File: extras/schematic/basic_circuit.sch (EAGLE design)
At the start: 2 parts, among them M1 ARDUINO-PRO-MINI-3.3V

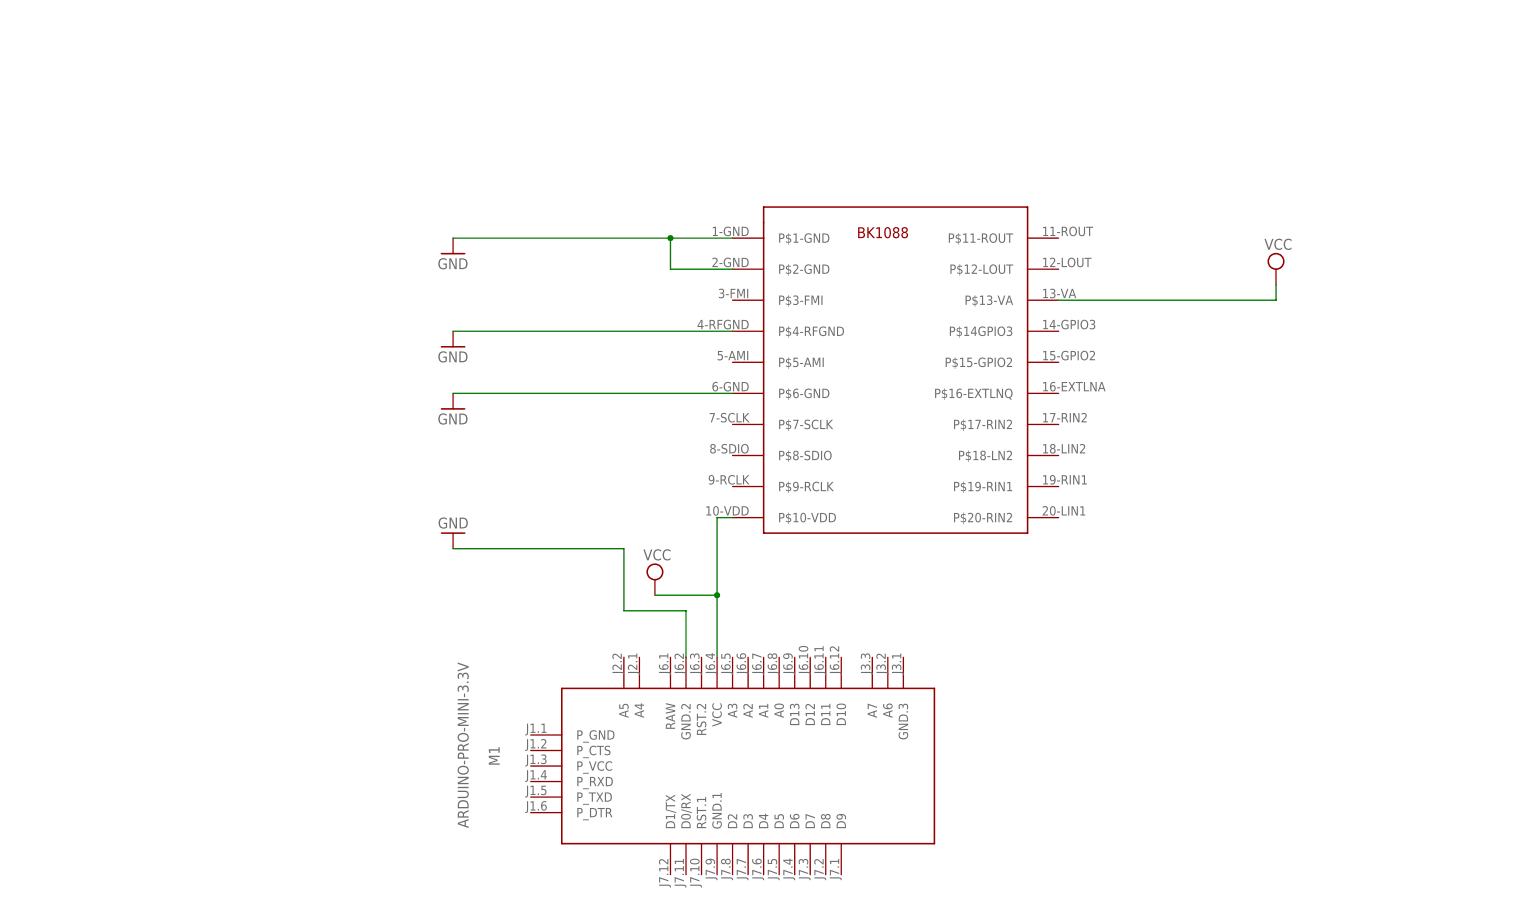
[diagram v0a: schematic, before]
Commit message: BK108X Arduino Library
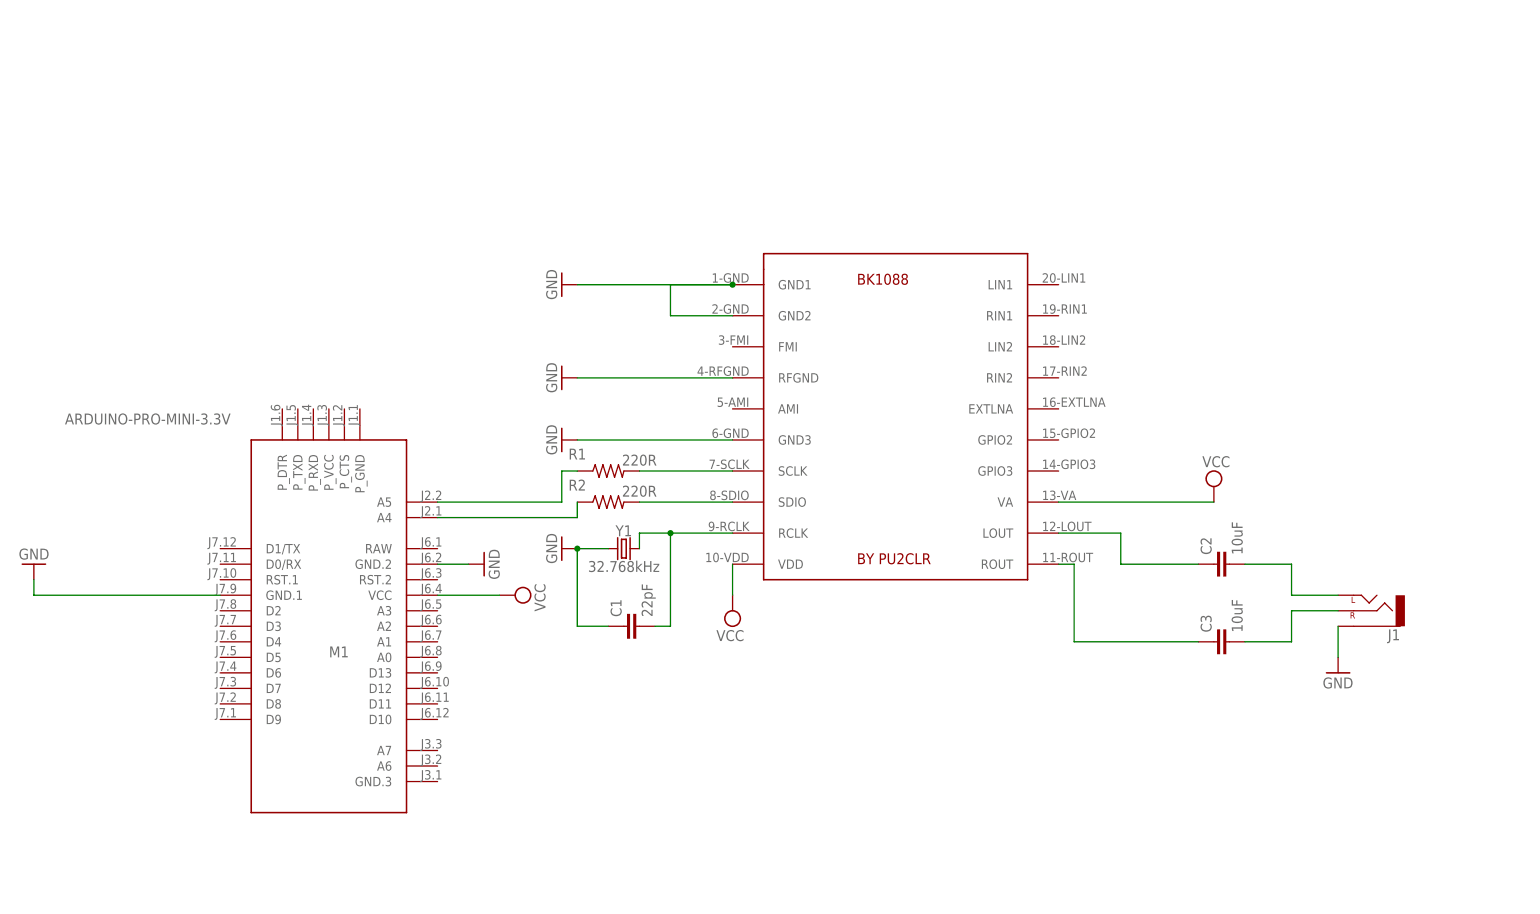
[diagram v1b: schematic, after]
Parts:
- added C1: 22pF, SparkFun-Capacitors:22PF-0603-50V-5%
- added C2, C3: 10uF, SparkFun-Capacitors:10UF-0603-6.3V-20%
- added J1: (no value), SparkFun-Connectors:AUDIO_JACK_2.5MMSPECIAL_POGO_PINS
- added R1, R2: 220R, Resistor:R-US_AXIAL-7.2MM-PITCH
- added Y1: 32.768kHz, SparkFun-Clocks:CRYSTAL-32.768KHZPTH-2X6
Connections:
- new net N$1: R1.2, U$1.SCLK
- new net N$2: R2.2, U$1.SDIO
- new net N$3: M1.A4, R2.1
- new net N$4: M1.A5, R1.1
- new net N$5: C1.2, U$1.RCLK, Y1.2
- new net N$6: C3.1, U$1.ROUT
- new net N$7: C2.1, U$1.LOUT
- new net N$8: C3.2, J1.RIGHT
- new net N$9: C2.2, J1.LEFT
- net GND: now also C1.1, J1.SLEEVE, M1.GND.1, U$1.GND1, U$1.GND2, U$1.GND3, U$1.RFGND, Y1.1; no longer U$1.P$1-GND, U$1.P$2-GND, U$1.P$4-RFGND, U$1.P$6-GND
- net VCC: now also U$1.VA, U$1.VDD; no longer U$1.P$10-VDD, U$1.P$13-VA
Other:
- moved on the sheet: M1

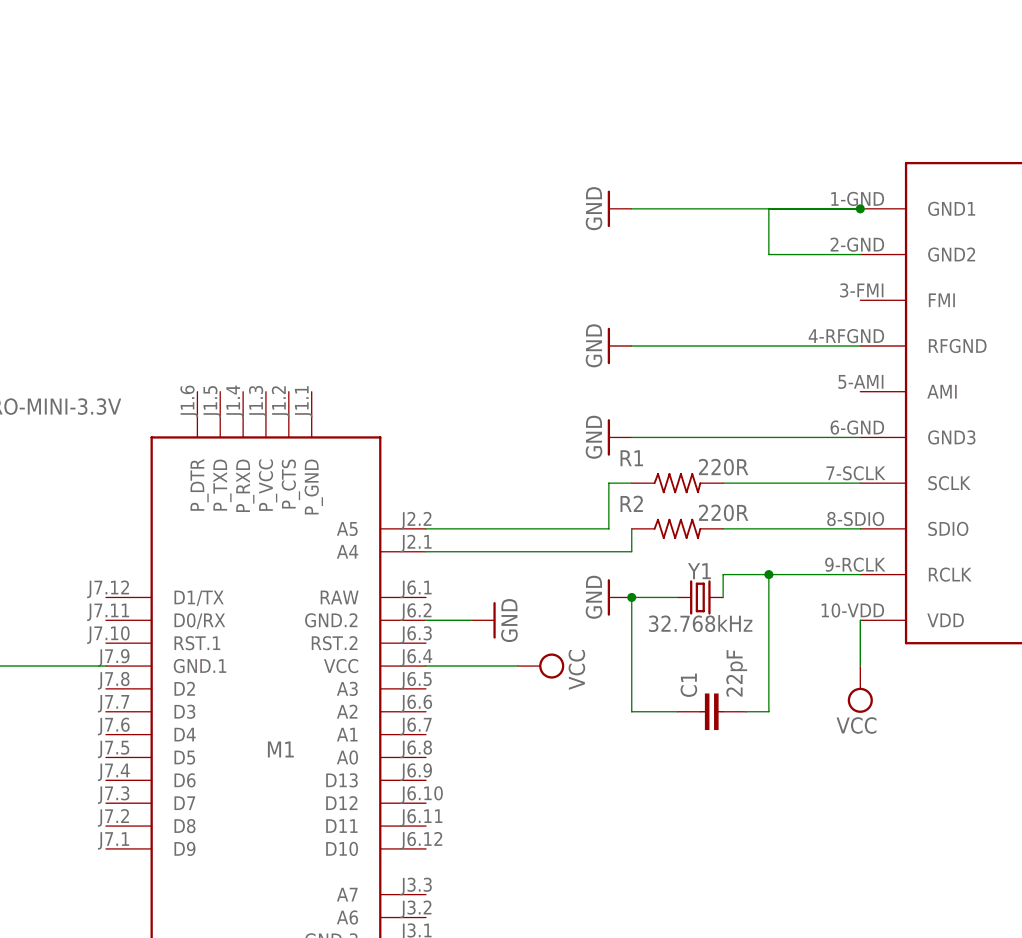
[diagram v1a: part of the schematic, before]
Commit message: BK1088 Arduino Library
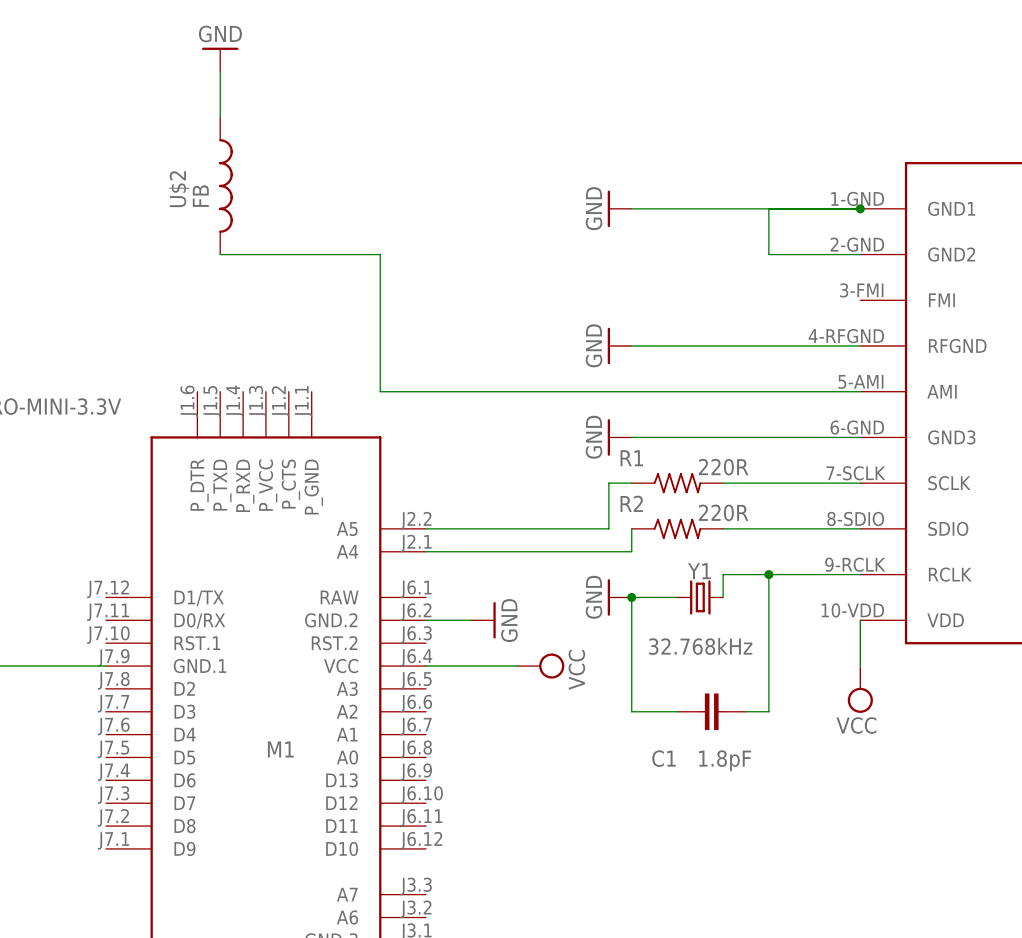
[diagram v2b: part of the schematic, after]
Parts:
- added U$2: FB, adafruit:FB
- C1: value 22pF -> 1.8pF; device SparkFun-Capacitors:22PF-0603-50V-5% -> capacitor-wima:C5/3
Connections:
- new net N$10: U$1.AMI, U$2.2
- net GND: now also U$2.1
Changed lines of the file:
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@@
 <part name="GND4" library="supply1" library_urn="urn:adsk.eagle:library:371" deviceset="GND" device=""/>
 <part name="Y1" library="SparkFun-Clocks" library_urn="urn:adsk.eagle:library:511" deviceset="CRYSTAL-32.768KHZ" device="PTH-2X6" package3d_urn="urn:adsk.eagle:package:37514/1" value="32.768kHz"/>
-<part name="C1" library="SparkFun-Capacitors" library_urn="urn:adsk.eagle:library:510" deviceset="22PF" device="-0603-50V-5%" package3d_urn="urn:adsk.eagle:package:37414/1" value="22pF"/>
 <part name="C2" library="SparkFun-Capacitors" library_urn="urn:adsk.eagle:library:510" deviceset="10UF" device="-0603-6.3V-20%" package3d_urn="urn:adsk.eagle:package:37414/1" value="10uF"/>
 <part name="C3" library="SparkFun-Capacitors" library_urn="urn:adsk.eagle:library:510" deviceset="10UF" device="-0603-6.3V-20%" package3d_urn="urn:adsk.eagle:package:37414/1" value="10uF"/>
@@
 <part name="SUPPLY1" library="supply2" library_urn="urn:adsk.eagle:library:372" deviceset="VCC" device=""/>
 <part name="GND7" library="supply1" library_urn="urn:adsk.eagle:library:371" deviceset="GND" device=""/>
+<part name="C1" library="capacitor-wima" library_urn="urn:adsk.eagle:library:116" deviceset="C" device="5/3" package3d_urn="urn:adsk.eagle:package:5433/1" value="1.8pF"/>
+<part name="U$2" library="adafruit" library_urn="urn:adsk.eagle:library:420" deviceset="FB" device="" package3d_urn="urn:adsk.eagle:package:6240653/1"/>
+<part name="GND8" library="supply1" library_urn="urn:adsk.eagle:library:371" deviceset="GND" device=""/>
 </parts>
 <sheets>
@@
 <instance part="Y1" gate="G$1" x="30.48" y="33.02" smashed="yes">
 <attribute name="NAME" x="30.48" y="35.052" size="1.778" layer="95" font="vector" align="bottom-center"/>
-<attribute name="VALUE" x="30.48" y="30.988" size="1.778" layer="96" font="vector" align="top-center"/>
-</instance>
-<instance part="C1" gate="G$1" x="33.02" y="20.32" smashed="yes" rot="R90">
-<attribute name="NAME" x="30.099" y="21.844" size="1.778" layer="95" font="vector" rot="R90"/>
-<attribute name="VALUE" x="35.179" y="21.844" size="1.778" layer="96" font="vector" rot="R90"/>
+<attribute name="VALUE" x="30.48" y="28.448" size="1.778" layer="96" font="vector" align="top-center"/>
 </instance>
 <instance part="C2" gate="G$1" x="129.54" y="30.48" smashed="yes" rot="R90">
@@
 <instance part="GND7" gate="1" x="7.62" y="30.48" smashed="yes" rot="R90">
 <attribute name="VALUE" x="10.16" y="27.94" size="1.778" layer="96" rot="R90"/>
+</instance>
+<instance part="C1" gate="G$1" x="30.48" y="20.32" smashed="yes" rot="R90">
+<attribute name="NAME" x="25.019" y="14.224" size="1.778" layer="95"/>
+<attribute name="VALUE" x="30.099" y="14.224" size="1.778" layer="96"/>
+</instance>
+<instance part="U$2" gate="G$1" x="-22.86" y="78.74" smashed="yes">
+<attribute name="NAME" x="-26.67" y="76.2" size="1.778" layer="95" rot="R90"/>
+<attribute name="VALUE" x="-24.13" y="76.2" size="1.778" layer="96" rot="R90"/>
+</instance>
+<instance part="GND8" gate="1" x="-22.86" y="93.98" smashed="yes" rot="R180">
+<attribute name="VALUE" x="-20.32" y="96.52" size="1.778" layer="96" rot="R180"/>
 </instance>
 </instances>
@@
 <pinref part="M1" gate="G$1" pin="GND.2"/>
 <wire x1="5.08" y1="30.48" x2="0" y2="30.48" width="0.1524" layer="91"/>
+</segment>
+<segment>
+<pinref part="U$2" gate="G$1" pin="1"/>
+<pinref part="GND8" gate="1" pin="GND"/>
+<wire x1="-22.86" y1="86.36" x2="-22.86" y2="91.44" width="0.1524" layer="91"/>
 </segment>
 </net>
@@
 </segment>
 </net>
+<net name="N$10" class="0">
+<segment>
+<pinref part="U$1" gate="G$1" pin="AMI"/>
+<wire x1="48.26" y1="55.88" x2="-5.08" y2="55.88" width="0.1524" layer="91"/>
+<wire x1="-5.08" y1="55.88" x2="-5.08" y2="71.12" width="0.1524" layer="91"/>
+<pinref part="U$2" gate="G$1" pin="2"/>
+<wire x1="-5.08" y1="71.12" x2="-22.86" y2="71.12" width="0.1524" layer="91"/>
+</segment>
+</net>

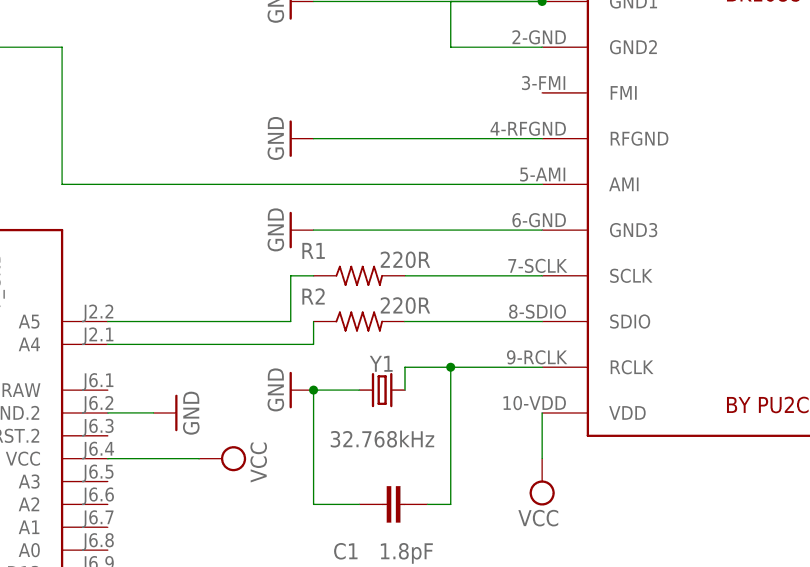
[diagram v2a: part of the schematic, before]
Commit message: BK1088 Arduino Library
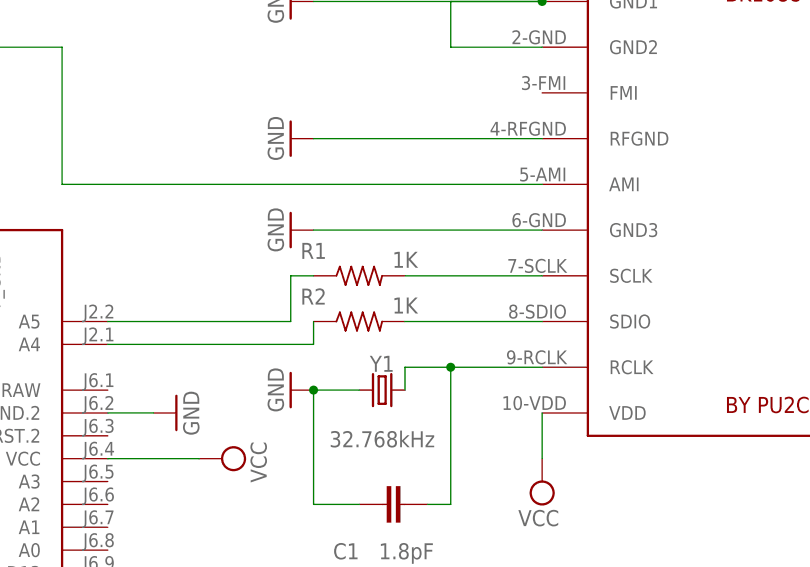
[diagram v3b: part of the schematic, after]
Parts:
- R1, R2: value 220R -> 1K
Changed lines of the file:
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@@
 <part name="U$1" library="BK1088" deviceset="BK1088" device="BK1088" package3d_urn="urn:adsk.eagle:package:22636398/1"/>
 <part name="GND3" library="supply1" library_urn="urn:adsk.eagle:library:371" deviceset="GND" device=""/>
-<part name="R1" library="Resistor" library_urn="urn:adsk.eagle:library:16378527" deviceset="R-US" device="AXIAL-7.2MM-PITCH" package3d_urn="urn:adsk.eagle:package:16378561/2" technology="_" value="220R"/>
-<part name="R2" library="Resistor" library_urn="urn:adsk.eagle:library:16378527" deviceset="R-US" device="AXIAL-7.2MM-PITCH" package3d_urn="urn:adsk.eagle:package:16378561/2" technology="_" value="220R"/>
+<part name="R1" library="Resistor" library_urn="urn:adsk.eagle:library:16378527" deviceset="R-US" device="AXIAL-7.2MM-PITCH" package3d_urn="urn:adsk.eagle:package:16378561/2" technology="_" value="1K"/>
+<part name="R2" library="Resistor" library_urn="urn:adsk.eagle:library:16378527" deviceset="R-US" device="AXIAL-7.2MM-PITCH" package3d_urn="urn:adsk.eagle:package:16378561/2" technology="_" value="1K"/>
 <part name="SUPPLY2" library="supply2" library_urn="urn:adsk.eagle:library:372" deviceset="VCC" device=""/>
 <part name="SUPPLY3" library="supply2" library_urn="urn:adsk.eagle:library:372" deviceset="VCC" device=""/>
